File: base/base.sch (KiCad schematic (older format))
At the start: 102 parts, among them J1 Screw_Terminal_01x02, J2 Out, Q2 MJD31C, Q3 IPD50R3K0CE, Q4 MJD31C, Q5 MMBTA42, Q6 MMBTA42, Q7 MMBTA42, Q8 MMBTA42, T1 FL2015-3LB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

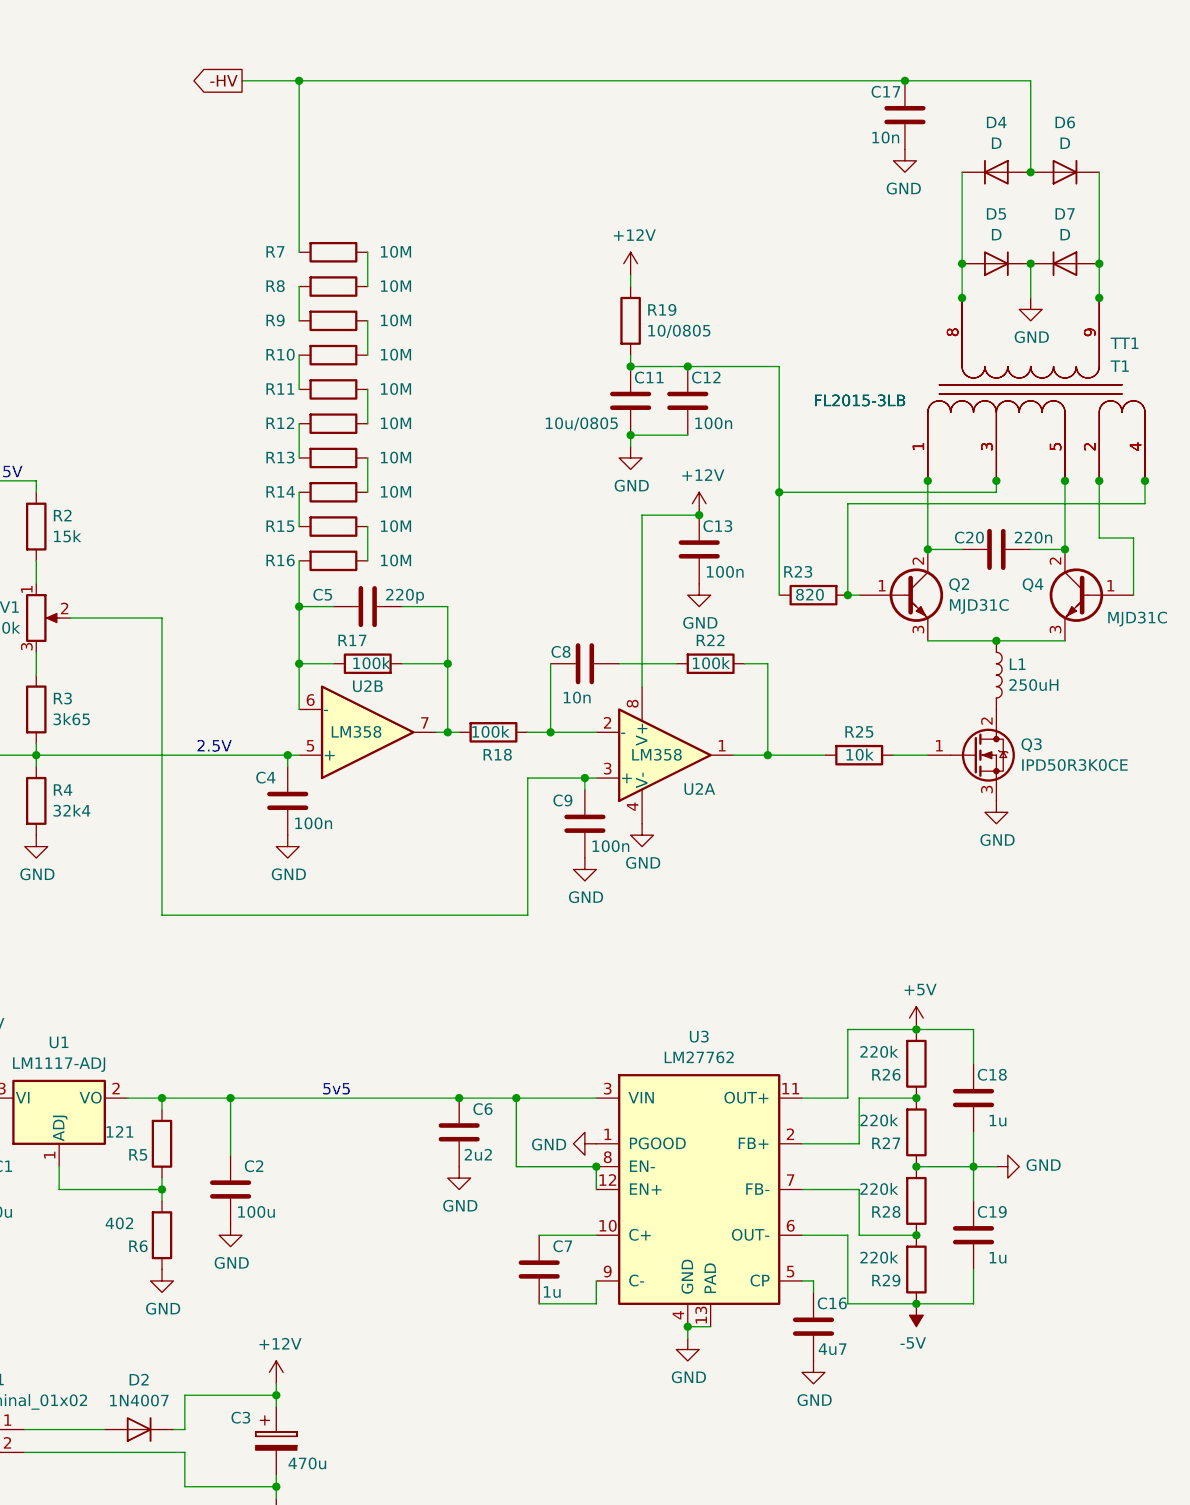
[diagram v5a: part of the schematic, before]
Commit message: Added testpoints
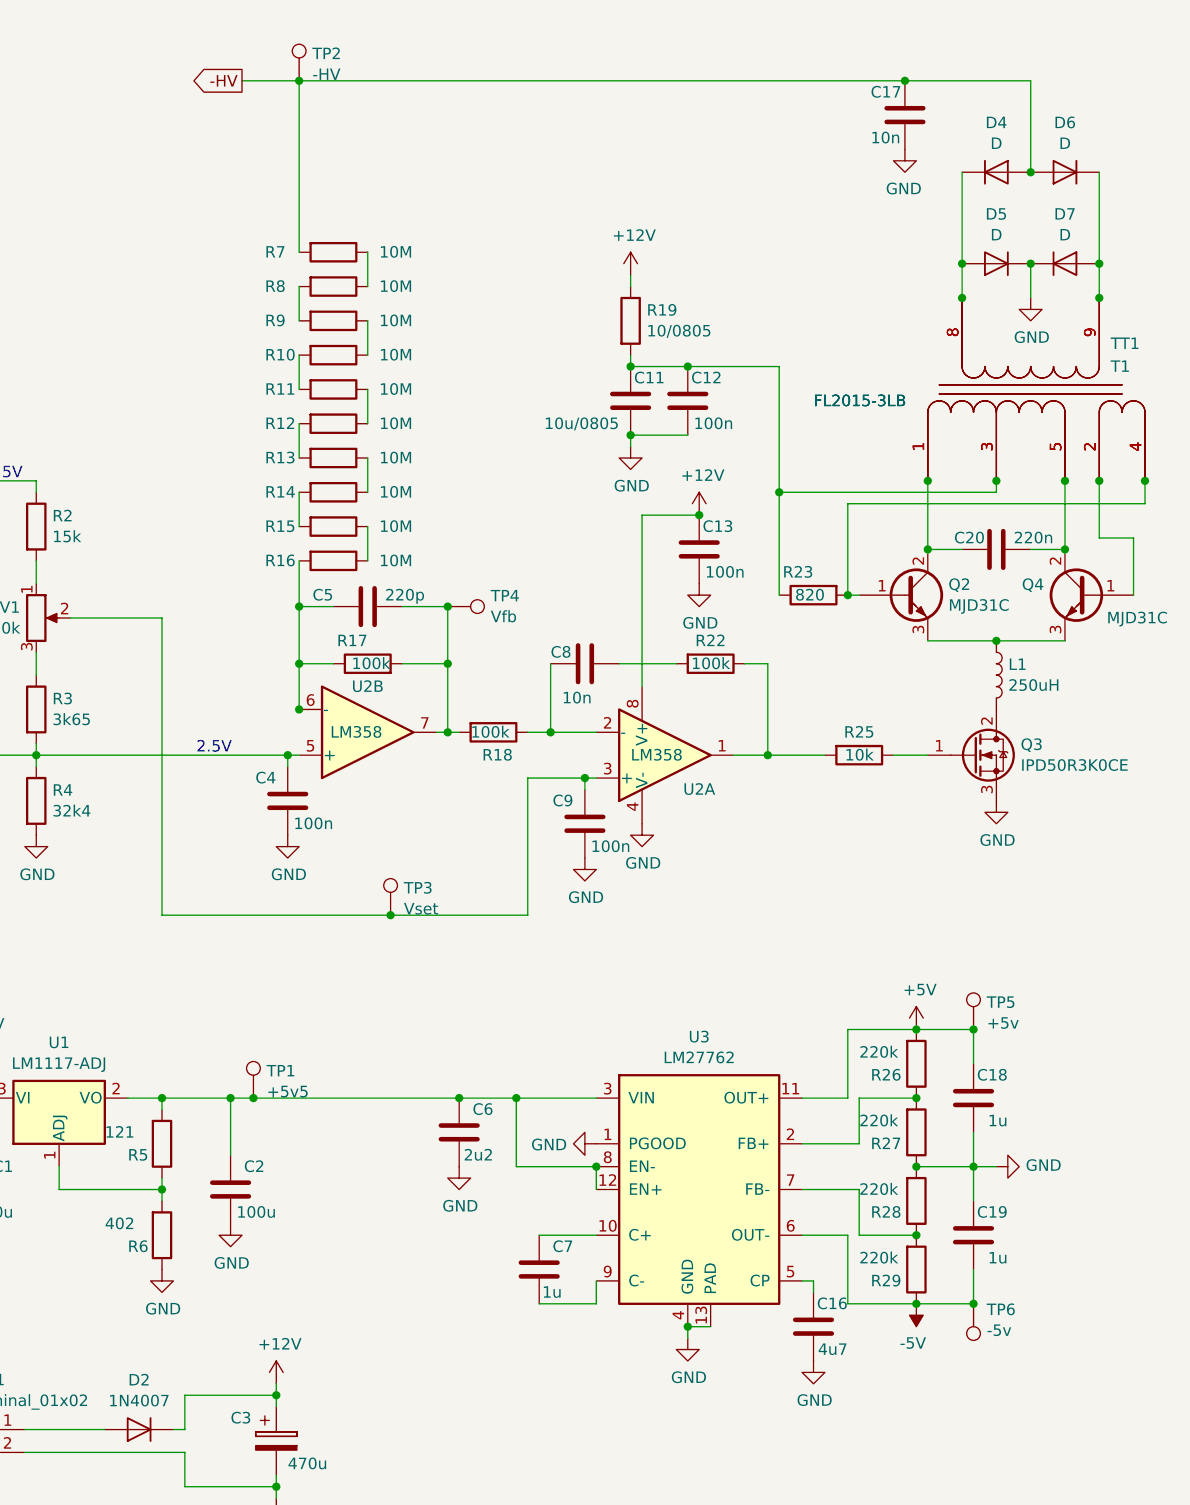
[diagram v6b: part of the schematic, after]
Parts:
- added TP1: +5v5, TestPoint:TestPoint_Pad_D1.5mm, symbol Connector:TestPoint
- added TP2: -HV, TestPoint:TestPoint_Pad_D1.5mm, symbol Connector:TestPoint
- added TP3: Vset, TestPoint:TestPoint_Pad_D1.5mm, symbol Connector:TestPoint
- added TP4: Vfb, TestPoint:TestPoint_Pad_D1.5mm, symbol Connector:TestPoint
- added TP5: +5v, TestPoint:TestPoint_Pad_D1.5mm, symbol Connector:TestPoint
- added TP6: -5v, TestPoint:TestPoint_Pad_D1.5mm, symbol Connector:TestPoint
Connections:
- net +5V: now also TP5.1
- net -5V: now also TP6.1
- net -HV: now also TP2.1
- net at C9.1, RV1.2, U2.3 (+): now also TP3.1
- net at C5.2, R17.2, R18.2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: now also TP4.1
- net at C2.1, C6.1, R5.2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: now also TP1.1
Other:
- note removed: "5v5"
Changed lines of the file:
@@
 	2050 5700 2050 5950
 Wire Wire Line
-	2050 5700 3050 5700
+	2050 5700 2150 5700
 $Comp
 L Device:C C19
@@
 	2300 4200 2300 4250
 Wire Wire Line
-	1750 4900 3350 4900
+	1750 4900 2750 4900
 Wire Wire Line
 	3350 4900 3350 4300
@@
 	3350 4300 3600 4300
 Connection ~ 3600 4300
-Text Notes 1900 4200 0    50   ~ 0
-2.5V
-Text Notes 1050 3000 0    50   ~ 0
-5V
 Wire Wire Line
 	650  2550 650  2650
@@
 $EndComp
 Connection ~ 2300 4200
-Wire Wire Line
-	1200 4200 2300 4200
 Wire Wire Line
 	1200 4200 1200 4250
@@
 	4050 2500 4450 2500
 Connection ~ 4450 3050
-Text Notes 2450 5700 0    50   ~ 0
-5v5
 Text GLabel 7550 5150 0    50   Input ~ 0
 -HV
@@
 	2350 1250 5000 1250
 Connection ~ 2350 1250
+Connection ~ 2150 5700
+Wire Wire Line
+	2150 5700 3050 5700
+Connection ~ 5300 5400
+Connection ~ 5300 6600
+Text Notes 1900 4200 0    50   ~ 0
+2.5V
+Text Notes 1050 3000 0    50   ~ 0
+5V
+$Comp
+L Connector:TestPoint TP6
+U 1 1 5D2D7222
+P 5300 6600
+F 0 "TP6" H 5242 6626 50  0000 R CNN
+F 1 "-5v" H 5242 6717 50  0000 R CNN
+F 2 "TestPoint:TestPoint_Pad_D1.5mm" H 5500 6600 50  0001 C CNN
+F 3 "~" H 5500 6600 50  0001 C CNN
+	1    5300 6600
+	-1   0    0    1
+$EndComp
+$Comp
+L Connector:TestPoint TP4
+U 1 1 5D2DE5A7
+P 3000 3550
+F 0 "TP4" V 2954 3738 50  0000 L CNN
+F 1 "Vfb" V 3045 3738 50  0000 L CNN
+F 2 "TestPoint:TestPoint_Pad_D1.5mm" H 3200 3550 50  0001 C CNN
+F 3 "~" H 3200 3550 50  0001 C CNN
+	1    3000 3550
+	0    1    1    0
+$EndComp
+Connection ~ 2350 4000
+$Comp
+L Connector:TestPoint TP1
+U 1 1 5D2CCAD5
+P 2150 5700
+F 0 "TP1" H 2208 5818 50  0000 L CNN
+F 1 "+5v5" H 2208 5727 50  0000 L CNN
+F 2 "TestPoint:TestPoint_Pad_D1.5mm" H 2350 5700 50  0001 C CNN
+F 3 "~" H 2350 5700 50  0001 C CNN
+	1    2150 5700
+	1    0    0    -1
+$EndComp
+$Comp
+L Connector:TestPoint TP5
+U 1 1 5D2D3A69
+P 5300 5400
+F 0 "TP5" H 5358 5518 50  0000 L CNN
+F 1 "+5v" H 5358 5427 50  0000 L CNN
+F 2 "TestPoint:TestPoint_Pad_D1.5mm" H 5500 5400 50  0001 C CNN
+F 3 "~" H 5500 5400 50  0001 C CNN
+	1    5300 5400
+	1    0    0    -1
+$EndComp
+Wire Wire Line
+	1200 4200 2300 4200
+$Comp
+L Connector:TestPoint TP2
+U 1 1 5D353874
+P 2350 1250
+F 0 "TP2" H 2408 1368 50  0000 L CNN
+F 1 "-HV" H 2408 1277 50  0000 L CNN
+F 2 "TestPoint:TestPoint_Pad_D1.5mm" H 2550 1250 50  0001 C CNN
+F 3 "~" H 2550 1250 50  0001 C CNN
+	1    2350 1250
+	1    0    0    -1
+$EndComp
+Connection ~ 3000 3550
+$Comp
+L Connector:TestPoint TP3
+U 1 1 5D378C91
+P 2750 4900
+F 0 "TP3" H 2808 5018 50  0000 L CNN
+F 1 "Vset" H 2808 4927 50  0000 L CNN
+F 2 "TestPoint:TestPoint_Pad_D1.5mm" H 2950 4900 50  0001 C CNN
+F 3 "~" H 2950 4900 50  0001 C CNN
+	1    2750 4900
+	1    0    0    -1
+$EndComp
+Connection ~ 2750 4900
+Wire Wire Line
+	2750 4900 3350 4900
 $EndSCHEMATC

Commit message: Added transformer 3d model
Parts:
- T1: footprint FL2015-3LB:FL2015-3LB -> FL2015-3LB:FL2015-4LB
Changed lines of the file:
@@
 F 0 "T1" V 5700 2300 50  0000 R CNN
 F 1 "FL2015-3LB" V 5550 3600 50  0000 R CNN
-F 2 "FL2015-3LB:FL2015-3LB" H 7250 1150 50  0001 C CNN
+F 2 "FL2015-3LB:FL2015-4LB" H 7250 1150 50  0001 C CNN
 F 3 "" H 7250 1150 50  0001 C CNN
 	1    5600 2600

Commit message: Library name juggling
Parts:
- removed T1: FL2015-3LB, FL2015-3LB:FL2015-4LB, symbol Device:FL2015-3LB
- removed TT1: FL2015-3LB, FL2015-3LB:G23736, symbol Device:FL2015-3LB
- added T1: FL2015, FL2015:FL2015-4LB, symbol FL2015:FL2015
- added TT1: FL2015, FL2015:G23736, symbol FL2015:FL2015
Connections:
- net at C20.1, Q2.2 (C): now also T1.1, TT1.1
- net at C20.2, Q4.2 (C): now also T1.5, TT1.5
- net at C11.1, C12.1, R19.2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: now also T1.3, TT1.3
- net at Q2.1 (B), R23.2: now also T1.4, TT1.4
- net at D4.1 (K), D5.2 (A): now also T1.8, TT1.8
- net at D6.1 (K), D7.2 (A): now also T1.9, TT1.9
- net at Q4.1 (B): now also T1.2, TT1.2
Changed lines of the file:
@@
 Wire Wire Line
 	4450 3050 5400 3050
-$Comp
-L Device:FL2015-3LB T1
-U 1 1 5D3AABDE
-P 5600 2600
-F 0 "T1" V 5700 2300 50  0000 R CNN
-F 1 "FL2015-3LB" V 5550 3600 50  0000 R CNN
-F 2 "FL2015-3LB:FL2015-4LB" H 7250 1150 50  0001 C CNN
-F 3 "" H 7250 1150 50  0001 C CNN
-	1    5600 2600
-	0    -1   -1   0
-$EndComp
 Wire Wire Line
 	5400 3700 5700 3700
@@
 Wire Wire Line
 	6000 3250 6000 3500
-$Comp
-L Device:FL2015-3LB TT1
-U 1 1 5CEA8266
-P 5600 2600
-F 0 "TT1" V 5800 2300 50  0000 R CNN
-F 1 "FL2015-3LB" V 5550 3600 50  0000 R CNN
-F 2 "FL2015-3LB:G23736" H 7250 1150 50  0001 C CNN
-F 3 "" H 7250 1150 50  0001 C CNN
-	1    5600 2600
-	0    -1   -1   0
-$EndComp
-Connection ~ 5100 3000
-Connection ~ 5850 3000
-Connection ~ 5400 3000
-Connection ~ 6050 3000
-Connection ~ 5700 3000
-Connection ~ 5250 2200
-Connection ~ 5850 2200
 Wire Wire Line
 	2350 1250 5000 1250
@@
 	0    1    1    0
 $EndComp
-Connection ~ 2350 4000
 $Comp
 L Connector:TestPoint TP1
@@
 Wire Wire Line
 	2750 4900 3350 4900
+$Comp
+L FL2015:FL2015 T1
+U 1 1 5CC8AA8F
+P 5600 2600
+F 0 "T1" V 5646 2062 50  0000 R CNN
+F 1 "FL2015" V 5555 2062 50  0000 R CNN
+F 2 "FL2015:FL2015-4LB" H 7250 1150 50  0001 C CNN
+F 3 "" H 7250 1150 50  0001 C CNN
+	1    5600 2600
+	0    -1   -1   0
+$EndComp
+$Comp
+L FL2015:FL2015 TT1
+U 1 1 5CC8DDE2
+P 5600 2600
+F 0 "TT1" V 5646 2062 50  0000 R CNN
+F 1 "FL2015" V 5555 2062 50  0000 R CNN
+F 2 "FL2015:G23736" H 7250 1150 50  0001 C CNN
+F 3 "" H 7250 1150 50  0001 C CNN
+	1    5600 2600
+	0    -1   -1   0
+$EndComp
+Connection ~ 5100 3000
+Connection ~ 5850 3000
+Connection ~ 5400 3000
+Connection ~ 6050 3000
+Connection ~ 5700 3000
+Connection ~ 5250 2200
+Connection ~ 5850 2200
 $EndSCHEMATC
